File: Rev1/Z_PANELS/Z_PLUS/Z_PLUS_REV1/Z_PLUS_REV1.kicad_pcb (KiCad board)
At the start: 2 copper layers, 98 x 98 mm, 62 parts, among them IC1 LTC4316IDD#PBF, IC2 SM141K08TFV, IC3 SM141K08TFV, IC4 SM141K08TFV, J1 F3311A7H121014E200, J2 73412-0114, J3 Tape_Measure_Antenna, Q1 BSS138, Q2 BSS138, Q3 MBT2222ADW1T1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

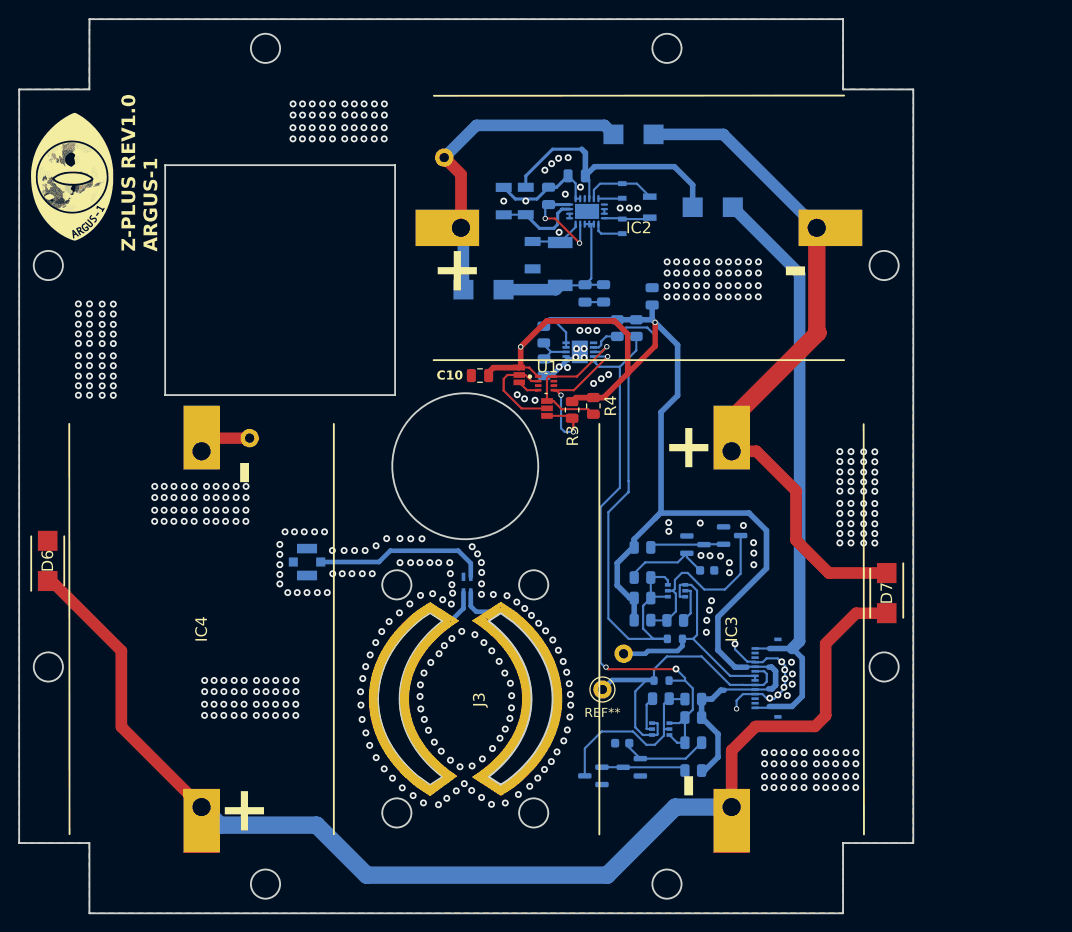
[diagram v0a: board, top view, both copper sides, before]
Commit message: updated ltc3130 schematic
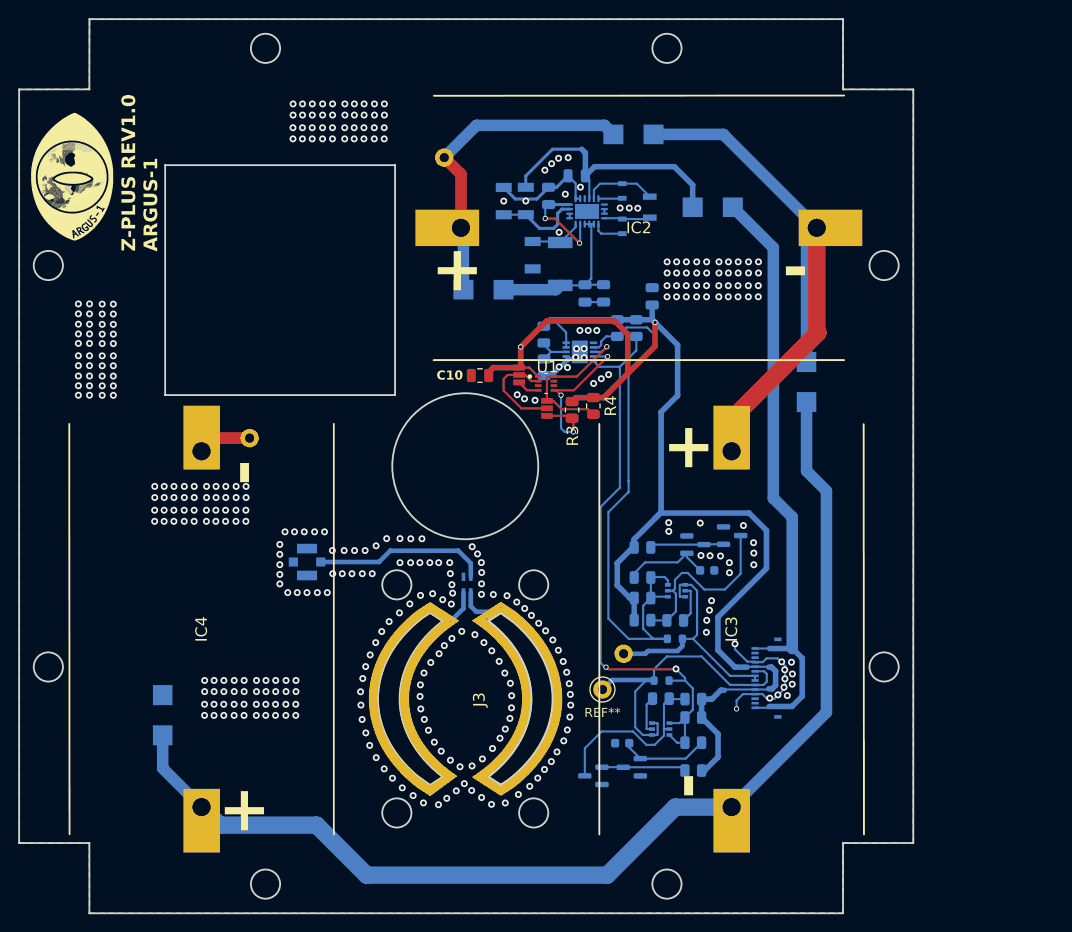
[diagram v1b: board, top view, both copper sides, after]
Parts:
- D6, D7: moved to B.Cu
- moved D7 24.8 mm to (207.1, 73.5)
- moved D6 21.1 mm to (136.5, 110.0)
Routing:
- net Net-(IC2-NEG): track 76.3 -> 65.8 mm
- net Net-(IC3-NEG): track 130.4 -> 123.5 mm
- net VSOLAR: track 67.2 -> 66.5 mm
- net GND: vias 462 -> 382

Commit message: updated boards
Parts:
- added C11: 47uF, Capacitor_SMD:C_0805_2012Metric, F.Cu at (232.5, 64.1)
- added D1: LSM115JE3_TR13, AA_AUTO_LOADER:DIOM5436X330N, F.Cu at (226.2, 65.3)
- added D2: LSM115JE3_TR13, AA_AUTO_LOADER:DIOM5436X330N, F.Cu at (226.2, 70.8)
- added D3: LSM115JE3_TR13, AA_AUTO_LOADER:DIOM5436X330N, F.Cu at (226.2, 76.3)
- added D4: LSM115JE3_TR13, AA_AUTO_LOADER:DIOM5436X330N, F.Cu at (226.2, 81.8)
- added D5: LSM115JE3_TR13, AA_AUTO_LOADER:DIOM5436X330N, F.Cu at (226.2, 87.3)
- C1, C2: value 10nF -> 0.1uF; footprint Capacitor_SMD:C_0603_1608Metric -> Capacitor_SMD:C_0805_2012Metric
- C10, C9: value 0.1uF -> CGA3E2X7R1H223K080AA; footprint Capacitor_SMD:C_0805_2012Metric -> AA_AUTO_LOADER:CAPC1608X90N
- C3: value 47uF -> 10nF; footprint Capacitor_SMD:C_0805_2012Metric -> Capacitor_SMD:C_0603_1608Metric
- C4: value 1uF -> 10nF; footprint Capacitor_SMD:C_0805_2012Metric -> Capacitor_SMD:C_0603_1608Metric
- C6: value CGA3E2X7R1H223K080AA -> 47uF; footprint AA_AUTO_LOADER:CAPC1608X90N -> Capacitor_SMD:C_0805_2012Metric
- C7: value CGA3E2X7R1H223K080AA -> 1uF; footprint AA_AUTO_LOADER:CAPC1608X90N -> Capacitor_SMD:C_0805_2012Metric
- J1: value F3311A7H121014E200 -> 73412-0114; footprint AA_AUTO_LOADER:F3311A7H121014E200 -> AA_AUTO_LOADER:73412-0110
- J2: value 73412-0114 -> Tape_Measure_Antenna; footprint AA_AUTO_LOADER:73412-0110 -> Audio_Module:Radio_antenna; moved to F.Cu
- J3: value Tape_Measure_Antenna -> F3311A7H121014E200; footprint Audio_Module:Radio_antenna -> AA_AUTO_LOADER:F3311A7H121014E200
- moved J2 24.6 mm to (171.7, 108.3), turned to 90 degrees
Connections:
- C1 pad 1: Net-(Q2-G) -> +3.3V
- C10 pad 1: +3.3V -> Net-(U2-SW2)
- C10 pad 2: GND -> Net-(U2-BST2)
- C2 pad 1: Net-(Q5-G) -> +3.3V
- C3 pad 1: Net-(U2-PVIN) -> Net-(Q2-G)
- C4 pad 1: Net-(U2-PVIN) -> Net-(Q5-G)
- C5 pad 1: Net-(U2-VCC) -> Net-(U2-PVIN)
- C6 pad 1: Net-(U2-SW1) -> Net-(U2-PVIN)
- C6 pad 2: Net-(U2-BST1) -> GND
- C7 pad 1: Net-(U2-SW2) -> Net-(U2-PVIN)
- C7 pad 2: Net-(U2-BST2) -> GND
- C8 pad 1: Net-(U2-VOUT) -> Net-(U2-VCC)
- C9 pad 1: +3.3V -> Net-(U2-SW1)
- C9 pad 2: GND -> Net-(U2-BST1)
- FL1 pad 1: Net-(J2-SIGNAL) -> Net-(J1-SIGNAL)
- IC2 pad 1: /SOLAR_PANEL_ELECTRONICS/7023_vout -> Net-(IC2-POS)
- IC2 pad 2: Net-(IC2-NEG) -> GND
- IC3 pad 1: Net-(IC2-NEG) -> Net-(IC3-POS)
- IC3 pad 2: Net-(IC3-NEG) -> Net-(IC2-POS)
- IC4 pad 1: Net-(IC3-NEG) -> /SOLAR_PANEL_ELECTRONICS/7023_vout
- IC4 pad 2: GND -> Net-(IC3-POS)
- J1 pad 1: VSOLAR -> Net-(J1-SIGNAL)
- J1 pad 2: unconnected-(J1-Pad2) -> GND
- J1 pad 3: unconnected-(J1-Pad3) -> GND
- J2 pad 1: Net-(J2-SIGNAL) -> Net-(FL1-Pad2)
- J2 pad 2: GND -> Net-(FL1-Pad3)
- J3 pad 1: Net-(FL1-Pad2) -> VSOLAR
- J3 pad 2: Net-(FL1-Pad3) -> unconnected-(J3-Pad2)
- U2 pad 9: /SOLAR_PANEL_ELECTRONICS/FB1 -> Net-(U2-VCC)
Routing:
- net Net-(J2-SIGNAL): track 19.0 -> 0.00 mm
- net Net-(J1-SIGNAL): track 0.00 -> 19.0 mm

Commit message: Z PLUS Updated
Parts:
- removed ? (x3): , 
- removed D10, D6, D7, D8, D9: LSM115JE3_TR13, AA_AUTO_LOADER:DIOM5436X330N
- removed R21: RV1206JR-0722ML, AA_AUTO_LOADER:RESC3116X65N
- removed R22: RC1206FR-072ML, AA_AUTO_LOADER:RESC3116X65N
- removed REF**: Test_Point_D1.02mm, Source_Footprints:Test_Point_D1.02mm
- added TP1: VSOLAR, TestPoint:TestPoint_Loop_D1.80mm_Drill1.0mm_Beaded, B.Cu at (207.1, 97.1)
- added TP2: GND, TestPoint:TestPoint_Loop_D1.80mm_Drill1.0mm_Beaded, B.Cu at (207.1, 101.0)
- added TP3: TestPoint, TestPoint:TestPoint_Loop_D1.80mm_Drill1.0mm_Beaded, F.Cu at (179.7, 86.9)
- added TP4: TestPoint, TestPoint:TestPoint_Loop_D1.80mm_Drill1.0mm_Beaded, F.Cu at (182.2, 82.5)
- C10, C11, D1, D2, D3, D4, D5, J3: moved to B.Cu
- moved J1 52.2 mm to (152.2, 93.3)
- moved C11 51.8 mm to (182.3, 51.1), turned to 180 degrees
- moved C4 51.6 mm to (198.2, 113.7), turned to 0 degrees
- moved D1 32.1 mm to (207.1, 91.1), turned to -90 degrees
- moved J3 31.1 mm to (202.8, 106.8), turned to -90 degrees
- moved Q4 29.7 mm to (185.2, 116.7), turned to 180 degrees
- moved C3 29.7 mm to (187.8, 93.0), turned to 180 degrees
- moved Q1 29.6 mm to (198.7, 91.2), turned to 0 degrees
- moved R7 27.0 mm to (187.8, 90.0), turned to 180 degrees
- moved D5 25.7 mm to (202.5, 97.5), turned to 90 degrees
- moved C10 25.2 mm to (186.4, 52.6), turned to -90 degrees
- moved Q5 25.0 mm to (189.2, 115.7), turned to 180 degrees
- moved Q2 24.5 mm to (194.5, 92.2), turned to 0 degrees
- moved R14 24.5 mm to (195.0, 115.4), turned to 0 degrees
- moved C2 23.3 mm to (195.0, 117.5), turned to 180 degrees
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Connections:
- net Net-(FL1-Pad2) renamed /1-
- net Net-(FL1-Pad3) renamed /1+
- U2 pad 17: unconnected-(U2-NC-Pad17) -> GND
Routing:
- net Net-(IC2-POS): track 0.00 -> 128.5 mm
- net Net-(IC3-NEG): track 123.5 -> 0.00 mm
- net Net-(IC3-POS): track 0.00 -> 91.6 mm
- net /SOLAR_PANEL_ELECTRONICS/7023_vout: track 35.8 -> 110.0 mm
- net Net-(IC2-NEG): track 65.8 -> 0.00 mm
- net VSOLAR: track 66.5 -> 20.5 mm
- net Net-(U2-VOUT): track 29.8 -> 71.7 mm
- net GND: track 45.5 -> 14.9 mm, vias 382 -> 381
- net +3.3V: track 155.7 -> 136.3 mm, vias 2 -> 4
- net Net-(U2-PVIN): track 19.1 -> 35.8 mm
- net SCL_SUN: track 64.1 -> 49.2 mm
- net Net-(U2-VCC): track 11.0 -> 23.1 mm, vias 2 -> 0
- net /SOLAR_PANEL_ELECTRONICS/FB1: track 9.43 -> 0.00 mm
- net SCL1_b4iso: track 35.1 -> 26.9 mm
- net SCL_4001: track 19.5 -> 27.4 mm
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- added copper zone on B.Cu, net Net-(U2-PVIN)
- added copper zone on B.Cu, net Net-(U2-SW1)
- added copper zone on B.Cu, net Net-(U2-SW2)
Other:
- board text added: "SCL_BISO"
- board text added: "SDA_BISO"
- board text removed: "TP1 SDA_BISO"
- board text removed: "TP2 SCL_BISO"

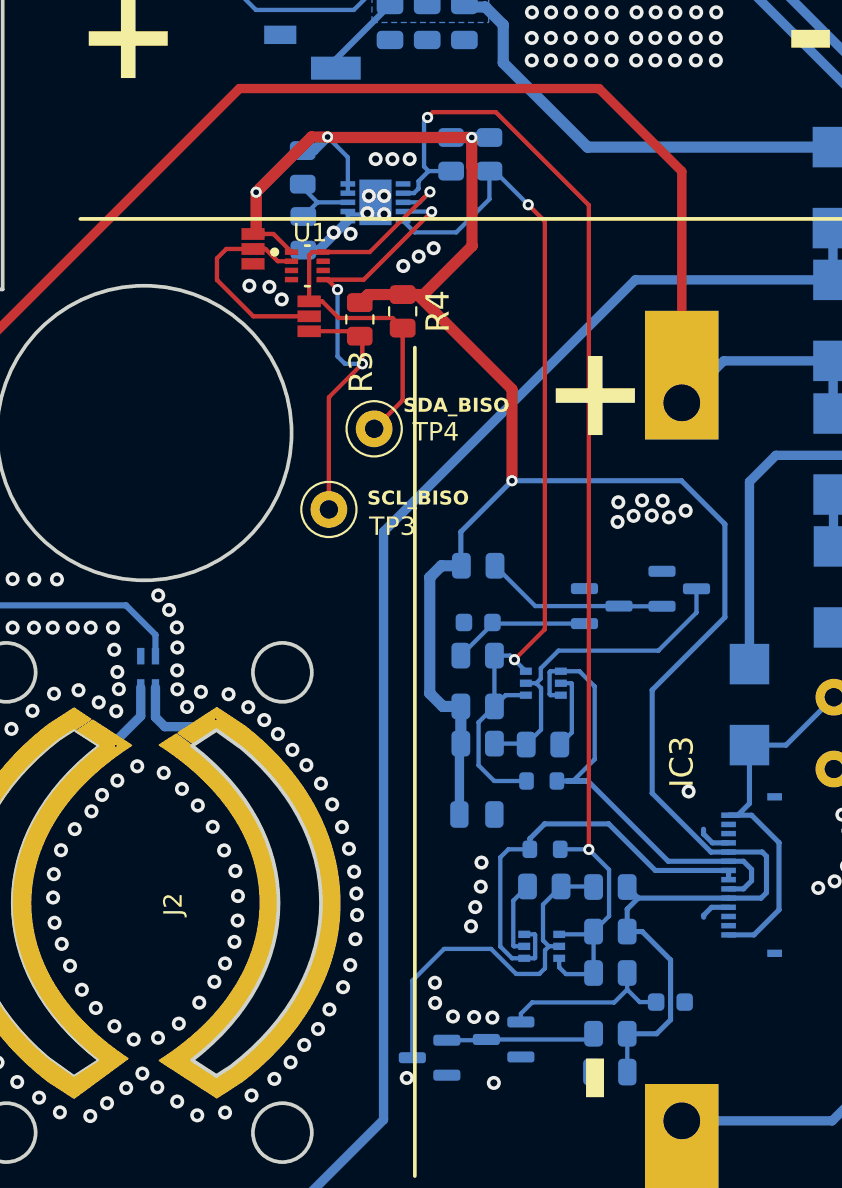
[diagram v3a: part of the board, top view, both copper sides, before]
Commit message: Z Plus DRCs cleared
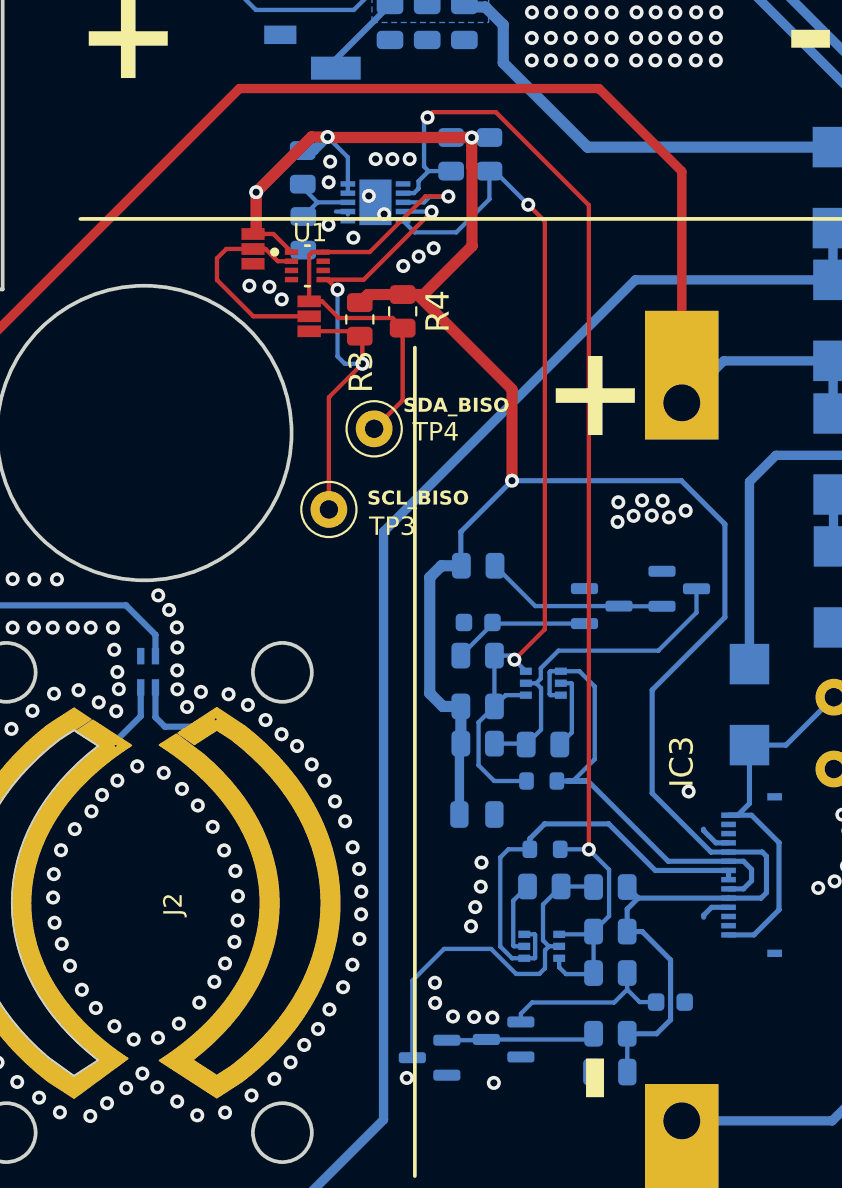
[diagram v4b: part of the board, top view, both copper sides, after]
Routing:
- net GND: track 14.9 -> 11.2 mm
- net SDA_4001: track 24.0 -> 25.8 mm
